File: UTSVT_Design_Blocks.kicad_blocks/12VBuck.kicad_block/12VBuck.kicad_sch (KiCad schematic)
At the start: 12 parts, among them U3 LMR51635XDDCR

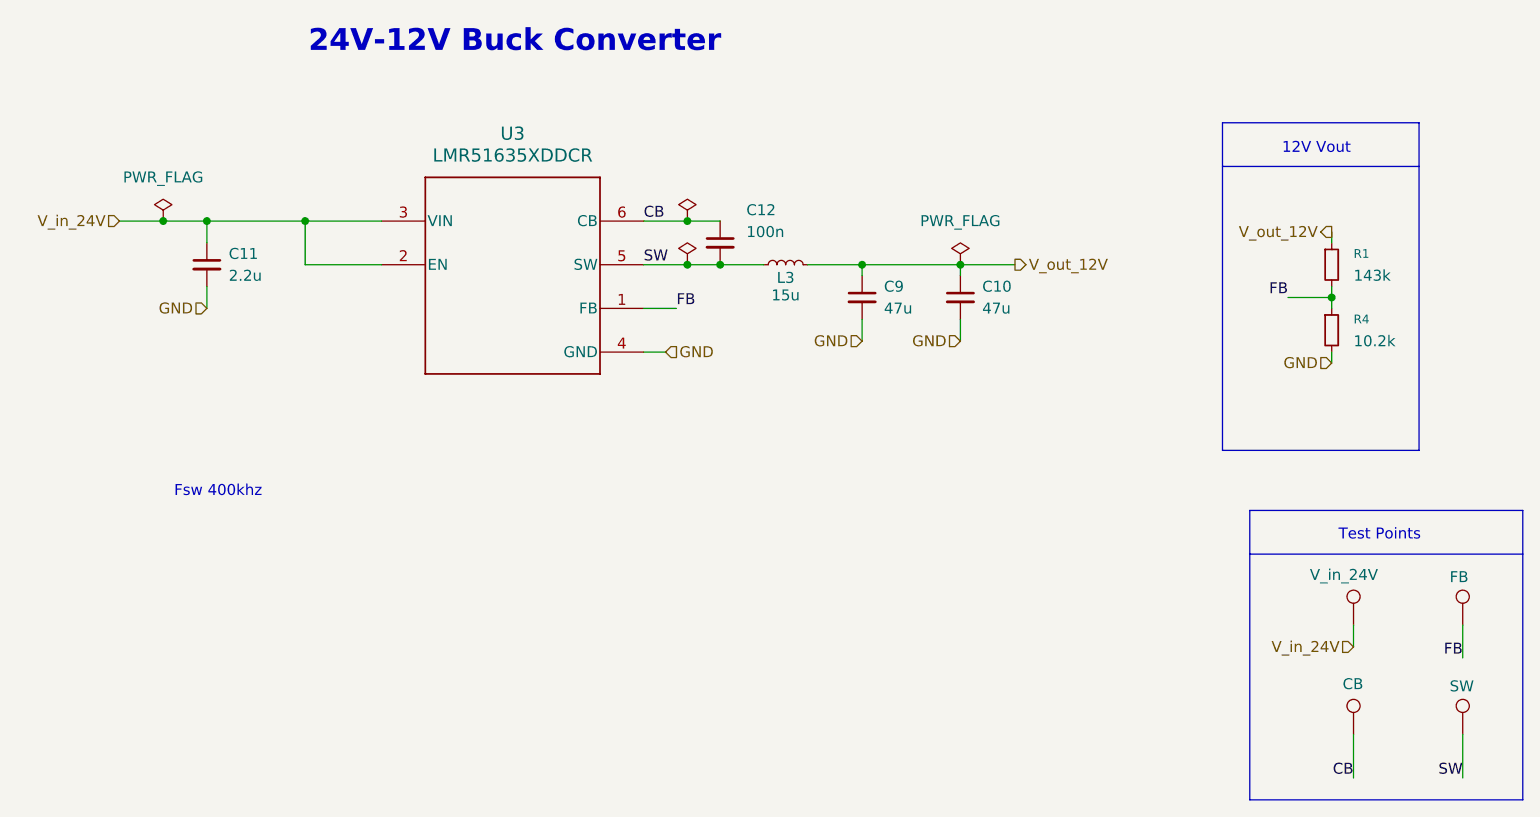
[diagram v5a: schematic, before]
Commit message: updated 5V/12V buck capacitor footprint (#58)
* updated 5V buck capacitor footprint

* 12V Buck update for capacitor footprint to 0603
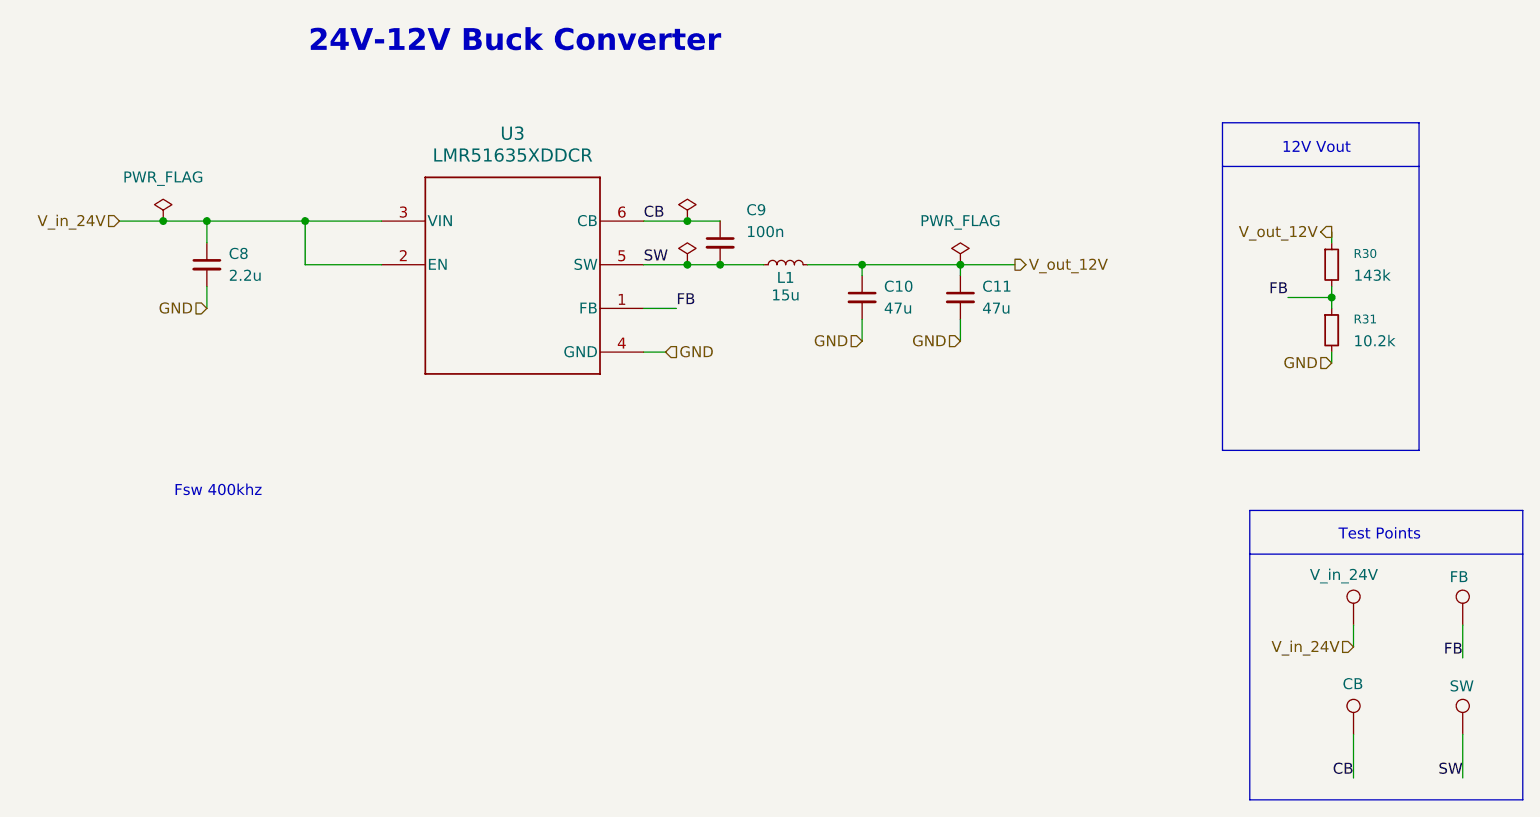
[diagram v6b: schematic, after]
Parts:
- C9: renamed from C12; footprint Resistor_SMD:R_0201_0603Metric_Pad0.64x0.40mm_HandSolder -> Capacitor_SMD:C_0603_1608Metric
- renumbered C9 to C10, C10 to C11, C11 to C8, L3 to L1, R1 to R30, R4 to R31, TP11 to TP10, TP14 to TP11, TP15 to TP12
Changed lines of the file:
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@@
 		(dnp no)
 		(fields_autoplaced yes)
-		(property "Reference" "C9"
+		(property "Reference" "C10"
 			(at 172.72 88.9062 0)
 			(effects
@@
 			(project "PS-Buck"
 				(path "/ad6c7df0-eb90-4670-9aa8-3e2007aefc2d/41c72b07-cf60-4ca9-96a7-6ae96aaa0c90"
-					(reference "C9")
+					(reference "C10")
 					(unit 1)
 				)
@@
 		(dnp no)
 		(fields_autoplaced yes)
-		(property "Reference" "#FLG013"
+		(property "Reference" "#FLG07"
 			(at 149.86 79.375 0)
 			(effects
@@
 			(project "PS-Buck"
 				(path "/ad6c7df0-eb90-4670-9aa8-3e2007aefc2d/41c72b07-cf60-4ca9-96a7-6ae96aaa0c90"
-					(reference "#FLG013")
+					(reference "#FLG07")
 					(unit 1)
 				)
@@
 		(dnp no)
 		(fields_autoplaced yes)
-		(property "Reference" "C11"
+		(property "Reference" "C8"
 			(at 96.52 85.0962 0)
 			(effects
@@
 			(project "PS-Buck"
 				(path "/ad6c7df0-eb90-4670-9aa8-3e2007aefc2d/41c72b07-cf60-4ca9-96a7-6ae96aaa0c90"
-					(reference "C11")
+					(reference "C8")
 					(unit 1)
 				)
@@
 		(on_board yes)
 		(dnp no)
-		(property "Reference" "L3"
+		(property "Reference" "L1"
 			(at 161.29 87.884 90)
 			(effects
@@
 			(project "PS-Buck"
 				(path "/ad6c7df0-eb90-4670-9aa8-3e2007aefc2d/41c72b07-cf60-4ca9-96a7-6ae96aaa0c90"
-					(reference "L3")
+					(reference "L1")
 					(unit 1)
 				)
@@
 		(on_board yes)
 		(dnp no)
-		(property "Reference" "TP14"
+		(property "Reference" "TP11"
 			(at 242.57 123.6979 0)
 			(effects
@@
 			(project "PowerPath"
 				(path "/ad6c7df0-eb90-4670-9aa8-3e2007aefc2d/41c72b07-cf60-4ca9-96a7-6ae96aaa0c90"
-					(reference "TP14")
+					(reference "TP11")
 					(unit 1)
 				)
@@
 		(on_board yes)
 		(dnp no)
-		(property "Reference" "TP11"
+		(property "Reference" "TP10"
 			(at 229.87 136.3979 0)
 			(effects
@@
 			(project "PowerPath"
 				(path "/ad6c7df0-eb90-4670-9aa8-3e2007aefc2d/41c72b07-cf60-4ca9-96a7-6ae96aaa0c90"
-					(reference "TP11")
+					(reference "TP10")
 					(unit 1)
 				)
@@
 		(on_board yes)
 		(dnp no)
-		(property "Reference" "TP15"
+		(property "Reference" "TP12"
 			(at 242.57 136.3979 0)
 			(effects
@@
 			(project "PowerPath"
 				(path "/ad6c7df0-eb90-4670-9aa8-3e2007aefc2d/41c72b07-cf60-4ca9-96a7-6ae96aaa0c90"
-					(reference "TP15")
+					(reference "TP12")
 					(unit 1)
 				)
@@
 		(dnp no)
 		(fields_autoplaced yes)
-		(property "Reference" "C10"
+		(property "Reference" "C11"
 			(at 184.15 88.9062 0)
 			(effects
@@
 			(project "PS-Buck"
 				(path "/ad6c7df0-eb90-4670-9aa8-3e2007aefc2d/41c72b07-cf60-4ca9-96a7-6ae96aaa0c90"
-					(reference "C10")
+					(reference "C11")
 					(unit 1)
 				)
@@
 		(dnp no)
 		(fields_autoplaced yes)
-		(property "Reference" "#FLG015"
+		(property "Reference" "#FLG09"
 			(at 181.61 84.455 0)
 			(effects
@@
 			(project "PS-Buck"
 				(path "/ad6c7df0-eb90-4670-9aa8-3e2007aefc2d/41c72b07-cf60-4ca9-96a7-6ae96aaa0c90"
-					(reference "#FLG015")
+					(reference "#FLG09")
 					(unit 1)
 				)
@@
 		(dnp no)
 		(fields_autoplaced yes)
-		(property "Reference" "#FLG011"
+		(property "Reference" "#FLG06"
 			(at 88.9 79.375 0)
 			(effects
@@
 			(project "PS-Buck"
 				(path "/ad6c7df0-eb90-4670-9aa8-3e2007aefc2d/41c72b07-cf60-4ca9-96a7-6ae96aaa0c90"
-					(reference "#FLG011")
+					(reference "#FLG06")
 					(unit 1)
 				)
@@
 		(on_board yes)
 		(dnp no)
-		(property "Reference" "C12"
+		(property "Reference" "C9"
 			(at 156.718 80.01 0)
 			(effects
@@
 			)
 		)
-		(property "Footprint" "Resistor_SMD:R_0201_0603Metric_Pad0.64x0.40mm_HandSolder"
+		(property "Footprint" "Capacitor_SMD:C_0603_1608Metric"
 			(at 153.67 83.82 0)
 			(effects
@@
 			(project "PS-Buck"
 				(path "/ad6c7df0-eb90-4670-9aa8-3e2007aefc2d/41c72b07-cf60-4ca9-96a7-6ae96aaa0c90"
-					(reference "C12")
+					(reference "C9")
 					(unit 1)
 				)
@@
 		(on_board yes)
 		(dnp no)
-		(property "Reference" "#FLG014"
+		(property "Reference" "#FLG08"
 			(at 149.86 84.455 0)
 			(effects
@@
 			(project "PS-Buck"
 				(path "/ad6c7df0-eb90-4670-9aa8-3e2007aefc2d/41c72b07-cf60-4ca9-96a7-6ae96aaa0c90"
-					(reference "#FLG014")
+					(reference "#FLG08")
 					(unit 1)
 				)
@@
 		(dnp no)
 		(fields_autoplaced yes)
-		(property "Reference" "R1"
+		(property "Reference" "R30"
 			(at 227.33 85.0899 0)
 			(effects
@@
 			(project "PS-Buck"
 				(path "/ad6c7df0-eb90-4670-9aa8-3e2007aefc2d/41c72b07-cf60-4ca9-96a7-6ae96aaa0c90"
-					(reference "R1")
+					(reference "R30")
 					(unit 1)
 				)
@@
 		(dnp no)
 		(fields_autoplaced yes)
-		(property "Reference" "R4"
+		(property "Reference" "R31"
 			(at 227.33 92.7099 0)
 			(effects
@@
 			(project "PS-Buck"
 				(path "/ad6c7df0-eb90-4670-9aa8-3e2007aefc2d/41c72b07-cf60-4ca9-96a7-6ae96aaa0c90"
-					(reference "R4")
-					(unit 1)
-				)
+					(reference "R31")
+					(unit 1)
+				)
